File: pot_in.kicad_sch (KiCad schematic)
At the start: 3 parts, among them J29 Conn_02x04_Odd_Even

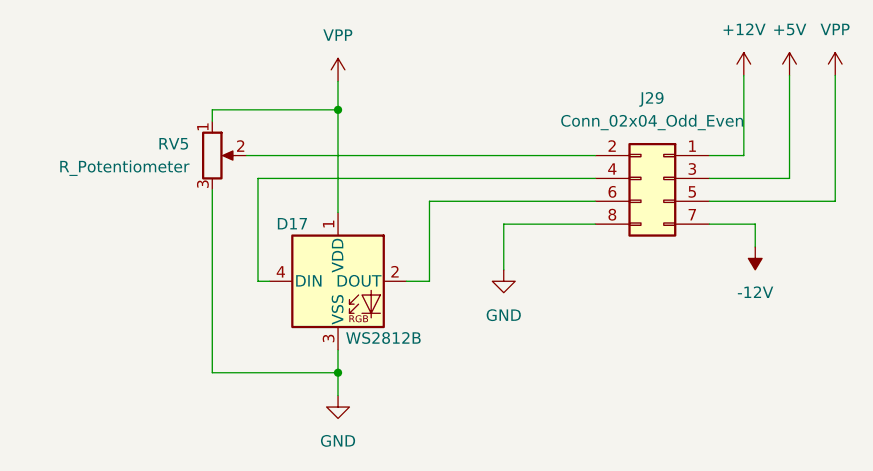
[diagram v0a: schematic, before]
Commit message: Switched to two layers
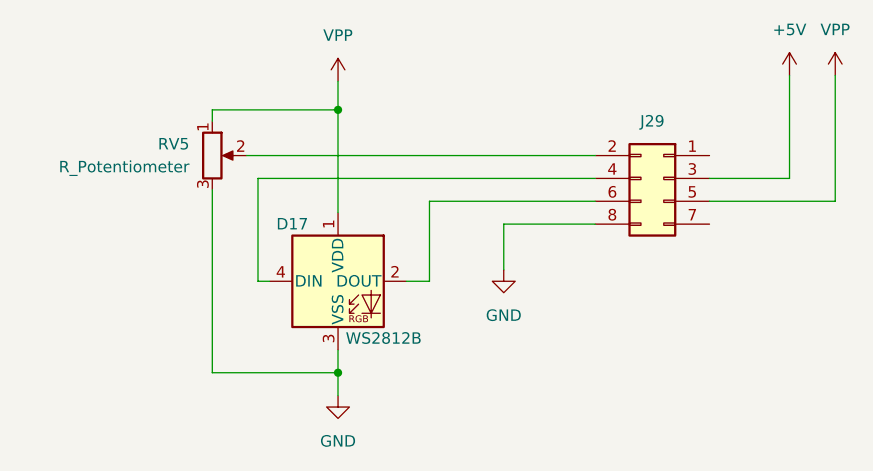
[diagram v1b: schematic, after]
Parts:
- J29: value Conn_02x04_Odd_Even -> (none)
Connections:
- net +12V: no longer names the net of J29.1 (Pin_1)
- net -12V: no longer names the net of J29.7 (Pin_7)
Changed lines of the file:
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@@
-    (stroke (width 0) (type default) (color 0 0 0 0))
-  )
-  (wire (pts (xy 136.525 83.82) (xy 136.525 86.36))
     (stroke (width 0) (type default) (color 0 0 0 0))
   )
@@
     (stroke (width 0) (type default) (color 0 0 0 0))
   )
-  (wire (pts (xy 131.445 83.82) (xy 136.525 83.82))
-    (stroke (width 0) (type default) (color 0 0 0 0))
-  )
   (wire (pts (xy 108.585 83.82) (xy 108.585 88.9))
     (stroke (width 0) (type default) (color 0 0 0 0))
@@
     (stroke (width 0) (type default) (color 0 0 0 0))
   )
-  (wire (pts (xy 135.255 67.31) (xy 135.255 76.2))
-    (stroke (width 0) (type default) (color 0 0 0 0))
-  )
   (wire (pts (xy 81.28 90.17) (xy 81.28 78.74))
     (stroke (width 0) (type default) (color 0 0 0 0))
   )
   (wire (pts (xy 82.55 90.17) (xy 81.28 90.17))
-    (stroke (width 0) (type default) (color 0 0 0 0))
-  )
-  (wire (pts (xy 131.445 76.2) (xy 135.255 76.2))
     (stroke (width 0) (type default) (color 0 0 0 0))
   )
@@
   (symbol (lib_id "Connector_Generic:Conn_02x04_Odd_Even") (at 126.365 78.74 0) (mirror y) (unit 1)
     (in_bom yes) (on_board yes) (fields_autoplaced)
-    (property "Reference" "J29" (id 0) (at 125.095 69.85 0))
-    (property "Value" "Conn_02x04_Odd_Even" (id 1) (at 125.095 72.39 0))
+    (property "Reference" "J29" (id 0) (at 125.095 72.39 0))
+    (property "Value" "" (id 1) (at 125.095 72.39 0)
+      (effects (font (size 1.27 1.27)) hide)
+    )
     (property "Footprint" "Connector_PinHeader_2.54mm:PinHeader_2x04_P2.54mm_Vertical" (id 2) (at 126.365 78.74 0)
       (effects (font (size 1.27 1.27)) hide)
@@
     (pin "1")
   )
-  (symbol (lib_id "power:-12V") (at 136.525 86.36 180) (unit 1)
-    (in_bom yes) (on_board yes) (fields_autoplaced)
-    (property "Reference" "#PWR0206" (id 0) (at 136.525 88.9 0)
-      (effects (font (size 1.27 1.27)) hide)
-    )
-    (property "Value" "-12V" (id 1) (at 136.525 91.44 0))
-    (property "Footprint" "" (id 2) (at 136.525 86.36 0)
-      (effects (font (size 1.27 1.27)) hide)
-    )
-    (property "Datasheet" "" (id 3) (at 136.525 86.36 0)
-      (effects (font (size 1.27 1.27)) hide)
-    )
-    (pin "1")
-  )
   (symbol (lib_id "power:VPP") (at 145.415 67.31 0) (unit 1)
     (in_bom yes) (on_board yes) (fields_autoplaced)
@@
       (effects (font (size 1.27 1.27)) hide)
     )
-    (pin "1")
-  )
-  (symbol (lib_id "power:+12V") (at 135.255 67.31 0) (unit 1)
-    (in_bom yes) (on_board yes) (fields_autoplaced)
-    (property "Reference" "#PWR0207" (id 0) (at 135.255 71.12 0)
-      (effects (font (size 1.27 1.27)) hide)
-    )
-    (property "Value" "+12V" (id 1) (at 135.255 62.23 0))
-    (property "Footprint" "" (id 2) (at 135.255 67.31 0)
-      (effects (font (size 1.27 1.27)) hide)
-    )
-    (property "Datasheet" "" (id 3) (at 135.255 67.31 0)
-      (effects (font (size 1.27 1.27)) hide)
-    )
